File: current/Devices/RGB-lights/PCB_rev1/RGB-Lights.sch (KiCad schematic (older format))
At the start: 22 parts

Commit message: updated stuff
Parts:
- renumbered SMD to SMD~fet, TO-220 to TO-220~fet
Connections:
- wire segments 92 -> 96
- no-connect marks 0 -> 20
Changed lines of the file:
@@
 $EndComp
 $Comp
-L Q_NJFET_DGS TO-220
+L Q_NJFET_DGS TO-220~fet
 U 1 1 56B7FA98
 P 6550 2150
@@
 $EndComp
 $Comp
-L Q_NJFET_DGS TO-220
+L Q_NJFET_DGS TO-220~fet
 U 1 1 56B7FAE0
 P 6100 2750
@@
 $EndComp
 $Comp
-L Q_NJFET_DGS TO-220
+L Q_NJFET_DGS TO-220~fet
 U 1 1 56B7FB14
 P 5600 3400
@@
 	1800 750  7300 750
 Wire Wire Line
-	4300 1350 4300 3250
-Wire Wire Line
 	4300 2250 4600 2250
 Connection ~ 4050 1350
@@
 Connection ~ 3500 2050
 $Comp
-L Q_NJFET_DGS SMD
+L Q_NJFET_DGS SMD~fet
 U 1 1 56B8A0F8
 P 6300 1800
@@
 $EndComp
 $Comp
-L Q_NJFET_DGS SMD
+L Q_NJFET_DGS SMD~fet
 U 1 1 56B8A1E4
 P 5900 2500
@@
 $EndComp
 $Comp
-L Q_NJFET_DGS SMD
+L Q_NJFET_DGS SMD~fet
 U 1 1 56B8A259
 P 5400 3750
@@
 	2000 2850 1900 2850
 Wire Wire Line
-	1900 2850 1900 1350
+	1900 1350 1900 3300
 Wire Wire Line
 	1800 2950 2000 2950
@@
 Wire Wire Line
 	5000 2550 4850 2550
+Wire Wire Line
+	4300 1350 4300 2250
+Wire Wire Line
+	1900 3300 3950 3300
+Wire Wire Line
+	3950 3300 3950 3200
+Wire Wire Line
+	3950 3200 4300 3200
+Wire Wire Line
+	4300 3200 4300 3250
+Connection ~ 1900 2850
+NoConn ~ 2000 2050
+NoConn ~ 2000 2150
+NoConn ~ 2000 2250
+NoConn ~ 2000 2350
+NoConn ~ 2000 2450
+NoConn ~ 2000 2550
+NoConn ~ 2000 2650
+NoConn ~ 2000 2750
+NoConn ~ 2000 3050
+NoConn ~ 2000 3150
+NoConn ~ 2500 3150
+NoConn ~ 2500 3050
+NoConn ~ 2500 2950
+NoConn ~ 2500 2750
+NoConn ~ 2500 2850
+NoConn ~ 2500 2650
+NoConn ~ 2500 2450
+NoConn ~ 2500 2250
+NoConn ~ 2500 2150
+NoConn ~ 2500 2050
 $EndSCHEMATC

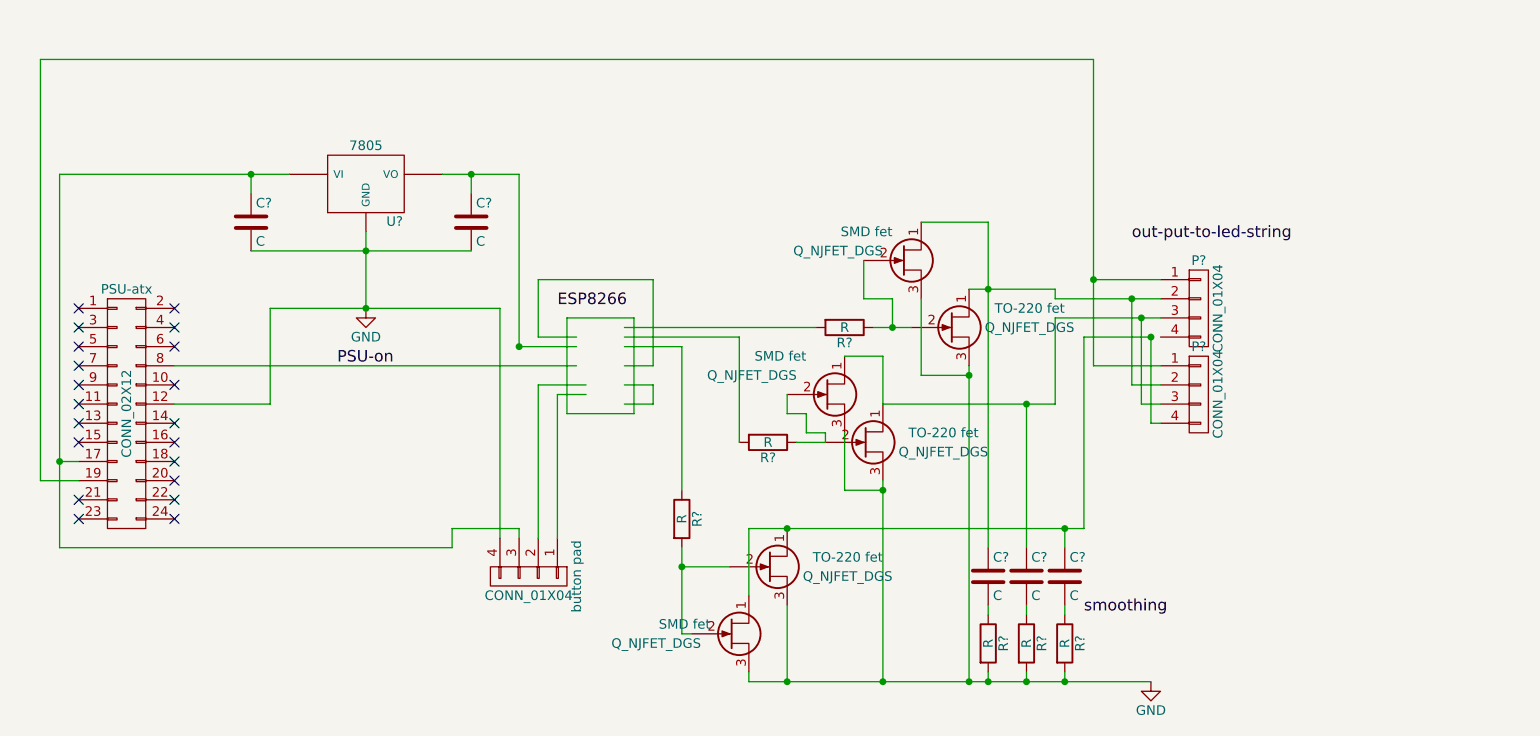
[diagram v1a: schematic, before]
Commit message: added a room sensor
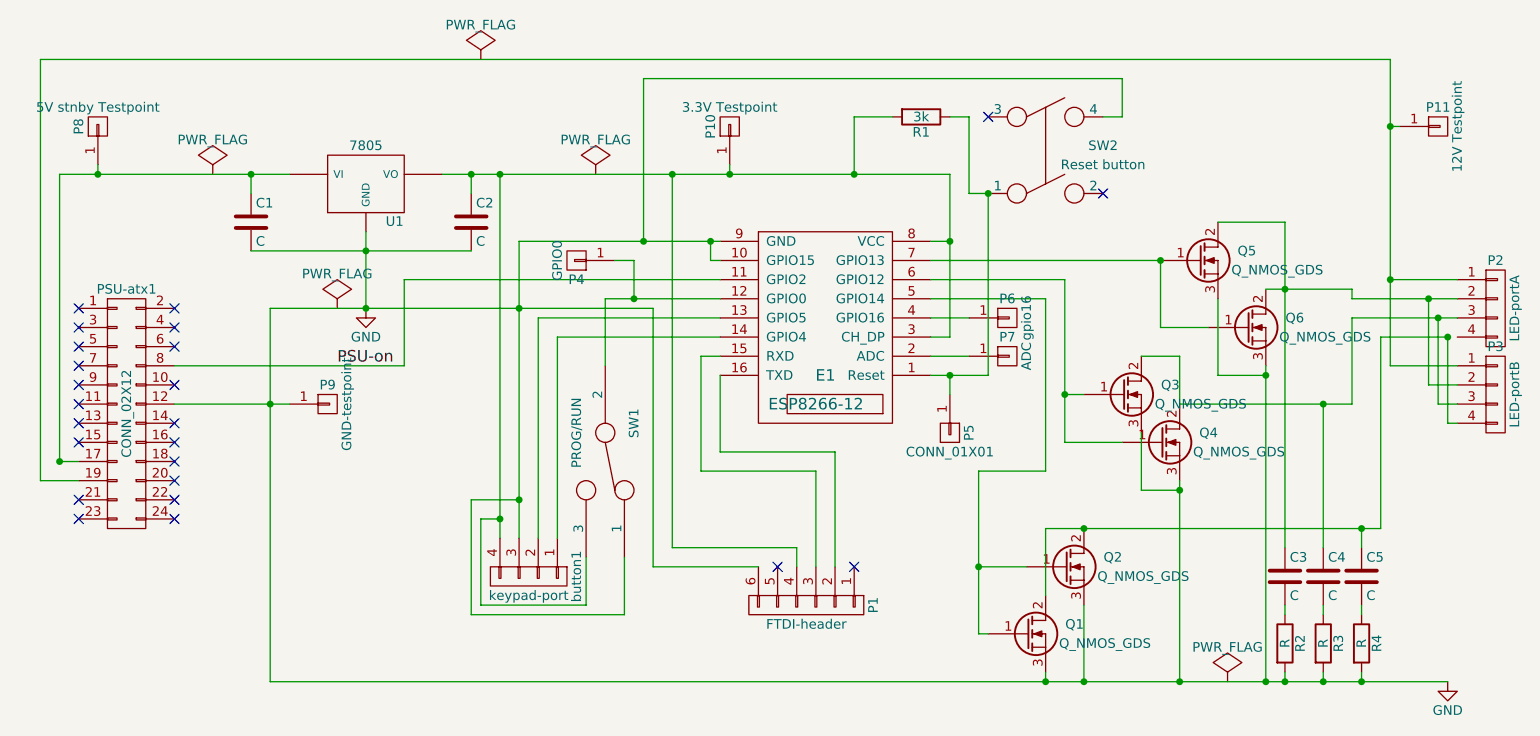
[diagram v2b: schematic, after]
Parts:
- removed R? (x3): R, symbol R
- removed SMD~fet (x3), TO-220~fet (x3): Q_NJFET_DGS, symbol Q_NJFET_DGS
- added E1: ESP8266-12, ESP8266:ESP-12, symbol ESP8266-12
- added P1: FTDI-header, Connect:Wafer_Horizontal17.5x5.8x7RM2.5-6, symbol CONN_01X06
- added P10: 3.3V Testpoint, Connect:1pin, symbol CONN_01X01
- added P11: 12V Testpoint, Connect:1pin, symbol CONN_01X01
- added P4: GPIO0, Connect:1pin, symbol CONN_01X01
- added P5: CONN_01X01, Connect:1pin, symbol CONN_01X01
- added P6: gpio16, Connect:1pin, symbol CONN_01X01
- added P7: ADC, Connect:1pin, symbol CONN_01X01
- added P8: 5V stnby Testpoint, Connect:1pin, symbol CONN_01X01
- added P9: GND-testpoint, Connect:1pin, symbol CONN_01X01
- added Q1, Q2, Q3, Q4, Q5, Q6: Q_NMOS_GDS, symbol Q_NMOS_GDS
- added R1: 3k, symbol R
- added SW1: PROG/RUN, symbol SWITCH_INV
- added SW2: Reset button, Buttons_Switches_SMD:SW_SPST_PTS645, symbol Switch_DPST
- C1, C2, C3, C4, C5: renamed from C?; footprint (none) -> Capacitors_ThroughHole:C_Rect_L7.5_W6.5_P5
- P2: renamed from P?; value CONN_01X04 -> LED-portA; footprint (none) -> Connect:bornier4
- P3: renamed from P?; value CONN_01X04 -> LED-portB; footprint (none) -> Connect:bornier4
- PSU-atx1: renamed from PSU-atx; footprint (none) -> ESP8266:ATX_90DEG
- button1: renamed from button~pad; value CONN_01X04 -> keypad-port; footprint (none) -> Connect:bornier4
- gave numbers to parts that had none: 4
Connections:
- net labels removed: ESP8266, out-put-to-led-string, smoothing
- wire segments 96 -> 123
- no-connect marks 20 -> 24
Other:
- moved on the sheet: C3, C4, C5, P2, P3, R2, R3, R4

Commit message: added new device
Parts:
- SW1: footprint (none) -> Buttons_Switches_SMD:SW_SPST_PTS645
- U1: footprint (none) -> Connect:PINHEAD1-3
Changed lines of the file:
@@
 F 0 "U1" H 3650 1204 50  0000 C CNN
 F 1 "7805" H 3500 1600 50  0000 C CNN
-F 2 "" H 3500 1400 50  0001 C CNN
+F 2 "Connect:PINHEAD1-3" H 3500 1400 50  0001 C CNN
 F 3 "" H 3500 1400 50  0000 C CNN
 	1    3500 1400
@@
 F 0 "SW1" H 4550 3000 50  0000 C CNN
 F 1 "PROG/RUN" H 4600 2700 50  0000 C CNN
-F 2 "" H 4750 2850 50  0001 C CNN
+F 2 "Buttons_Switches_SMD:SW_SPST_PTS645" H 4750 2850 50  0001 C CNN
 F 3 "" H 4750 2850 50  0000 C CNN
 	1    4750 2850

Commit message: updated stuff, yer
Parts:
- Q1, Q3, Q5: footprint (none) -> TO_SOT_Packages_SMD:TO-252-2Lead
- Q2, Q4, Q6: footprint (none) -> TO_SOT_Packages_THT:TO-220_Neutral123_Horizontal_LargePads
- R1, R2, R3, R4: footprint (none) -> Resistors_Universal:Resistor_SMD+THTuniversal_2512_RM10_HandSoldering_RevA_Date25Jun2010
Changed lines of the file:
@@
 LIBS:valves
 LIBS:esp8266-12
+LIBS:ESP8266
 LIBS:RGB-Lights-cache
 EELAYER 25 0
@@
 F 0 "R2" V 8380 3800 50  0000 C CNN
 F 1 "R" V 8300 3800 50  0000 C CNN
-F 2 "" V 8230 3800 50  0001 C CNN
+F 2 "Resistors_Universal:Resistor_SMD+THTuniversal_2512_RM10_HandSoldering_RevA_Date25Jun2010" V 8230 3800 50  0001 C CNN
 F 3 "" H 8300 3800 50  0000 C CNN
 	1    8300 3800
@@
 F 0 "R3" V 8580 3800 50  0000 C CNN
 F 1 "R" V 8500 3800 50  0000 C CNN
-F 2 "" V 8430 3800 50  0001 C CNN
+F 2 "Resistors_Universal:Resistor_SMD+THTuniversal_2512_RM10_HandSoldering_RevA_Date25Jun2010" V 8430 3800 50  0001 C CNN
 F 3 "" H 8500 3800 50  0000 C CNN
 	1    8500 3800
@@
 F 0 "R4" V 8780 3800 50  0000 C CNN
 F 1 "R" V 8700 3800 50  0000 C CNN
-F 2 "" V 8630 3800 50  0001 C CNN
+F 2 "Resistors_Universal:Resistor_SMD+THTuniversal_2512_RM10_HandSoldering_RevA_Date25Jun2010" V 8630 3800 50  0001 C CNN
 F 3 "" H 8700 3800 50  0000 C CNN
 	1    8700 3800
@@
 F 0 "R1" V 6480 1050 50  0000 C CNN
 F 1 "3k" V 6400 1050 50  0000 C CNN
-F 2 "" V 6330 1050 50  0001 C CNN
+F 2 "Resistors_Universal:Resistor_SMD+THTuniversal_2512_RM10_HandSoldering_RevA_Date25Jun2010" V 6330 1050 50  0001 C CNN
 F 3 "" H 6400 1050 50  0000 C CNN
 	1    6400 1050
@@
 F 0 "Q5" H 8150 1850 50  0000 R CNN
 F 1 "Q_NMOS_GDS" H 8500 1750 50  0000 R CNN
-F 2 "" H 8050 1900 50  0001 C CNN
+F 2 "TO_SOT_Packages_SMD:TO-252-2Lead" H 8050 1900 50  0001 C CNN
 F 3 "" H 7850 1800 50  0000 C CNN
 	1    7850 1800
@@
 F 0 "Q6" H 8400 2200 50  0000 R CNN
 F 1 "Q_NMOS_GDS" H 8750 2100 50  0000 R CNN
-F 2 "" H 8300 2250 50  0001 C CNN
+F 2 "TO_SOT_Packages_THT:TO-220_Neutral123_Horizontal_LargePads" H 8300 2250 50  0001 C CNN
 F 3 "" H 8100 2150 50  0000 C CNN
 	1    8100 2150
@@
 F 0 "Q3" H 7750 2550 50  0000 R CNN
 F 1 "Q_NMOS_GDS" H 8100 2450 50  0000 R CNN
-F 2 "" H 7650 2600 50  0001 C CNN
+F 2 "TO_SOT_Packages_SMD:TO-252-2Lead" H 7650 2600 50  0001 C CNN
 F 3 "" H 7450 2500 50  0000 C CNN
 	1    7450 2500
@@
 F 0 "Q4" H 7950 2800 50  0000 R CNN
 F 1 "Q_NMOS_GDS" H 8300 2700 50  0000 R CNN
-F 2 "" H 7850 2850 50  0001 C CNN
+F 2 "TO_SOT_Packages_THT:TO-220_Neutral123_Horizontal_LargePads" H 7850 2850 50  0001 C CNN
 F 3 "" H 7650 2750 50  0000 C CNN
 	1    7650 2750
@@
 F 0 "Q1" H 7250 3800 50  0000 R CNN
 F 1 "Q_NMOS_GDS" H 7600 3700 50  0000 R CNN
-F 2 "" H 7150 3850 50  0001 C CNN
+F 2 "TO_SOT_Packages_SMD:TO-252-2Lead" H 7150 3850 50  0001 C CNN
 F 3 "" H 6950 3750 50  0000 C CNN
 	1    6950 3750
@@
 F 0 "Q2" H 7450 3450 50  0000 R CNN
 F 1 "Q_NMOS_GDS" H 7800 3350 50  0000 R CNN
-F 2 "" H 7350 3500 50  0001 C CNN
+F 2 "TO_SOT_Packages_THT:TO-220_Neutral123_Horizontal_LargePads" H 7350 3500 50  0001 C CNN
 F 3 "" H 7150 3400 50  0000 C CNN
 	1    7150 3400
@@
 Connection ~ 2100 1350
 Connection ~ 7050 4000
+Connection ~ 3100 1350
+Connection ~ 3500 1650
+Connection ~ 3900 1350
 $EndSCHEMATC
